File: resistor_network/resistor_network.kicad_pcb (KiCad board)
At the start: 2 copper layers, 14 x 21 mm, 26 parts, among them J1 Vin_reg, J2 GND, J3 Vin_pow, J4 Conn_01x08, J5 Conn_01x08, Q1 BC847, Q2 BCX53

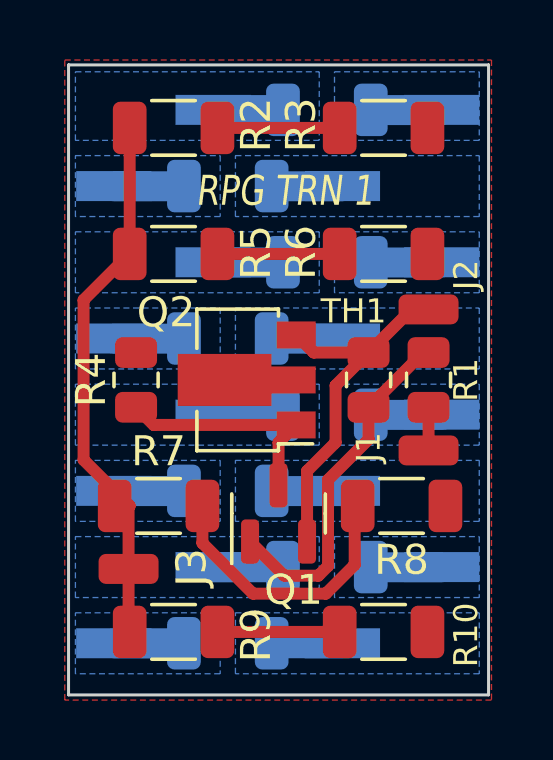
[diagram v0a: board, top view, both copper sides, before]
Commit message: New backplane, Reference Rev 0.6 with heated resistor network support
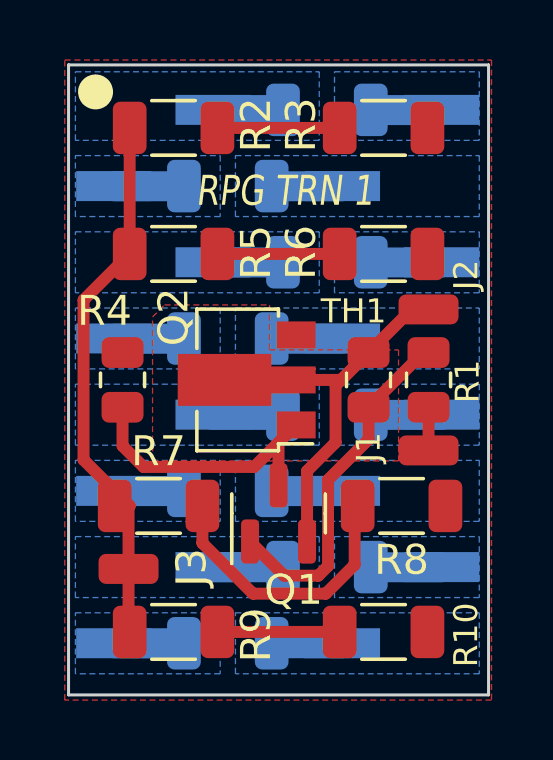
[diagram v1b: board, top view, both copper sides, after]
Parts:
- R1: value 680 -> 16k
- moved R4 0.45 mm to (136.8, 95.5)
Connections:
- Q2 pad 2: Net-(Q2-Pad2) -> Net-(J2-Pad1)
- Q2 pad 3: Net-(J2-Pad1) -> Net-(Q2-Pad3)
- R10 pad 2: Net-(Q2-Pad2) -> Net-(Q2-Pad3)
- R3 pad 2: Net-(Q2-Pad2) -> Net-(Q2-Pad3)
- R4 pad 1: Net-(Q2-Pad2) -> Net-(Q2-Pad3)
- R6 pad 2: Net-(Q2-Pad2) -> Net-(Q2-Pad3)
- R8 pad 2: Net-(Q2-Pad2) -> Net-(Q2-Pad3)
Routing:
- net Net-(Q1-Pad3): track 7.89 -> 10.3 mm
- added copper zone on F.Cu, net Net-(J2-Pad1)
- added copper zone on B.Cu, net Net-(J4-Pad1)
- added copper zone on B.Cu, net Net-(J4-Pad2)
- added copper zone on B.Cu, net Net-(J4-Pad3)
- added copper zone on B.Cu, net Net-(J4-Pad4)
- added copper zone on B.Cu, net Net-(J4-Pad5)
- added copper zone on B.Cu, net Net-(J4-Pad6)
- added copper zone on B.Cu, net Net-(J4-Pad7)
- added copper zone on B.Cu, net Net-(J4-Pad8)
- added copper zone on B.Cu, net Net-(J5-Pad1)
- added copper zone on B.Cu, net Net-(J5-Pad2)
- added copper zone on B.Cu, net Net-(J5-Pad3)
- added copper zone on B.Cu, net Net-(J5-Pad4)
- added copper zone on B.Cu, net Net-(J5-Pad5)
- added copper zone on B.Cu, net Net-(J5-Pad6)
- added copper zone on B.Cu, net Net-(J5-Pad7)
- added copper zone on B.Cu, net Net-(J5-Pad8)
- added copper zone on F.Cu, net Net-(Q2-Pad3)
- removed copper zone on B.Cu, net (none)
- removed copper zone on F.Cu, net Net-(Q2-Pad2)
